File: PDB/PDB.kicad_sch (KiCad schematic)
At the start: 74 parts, among them J11 swd, J12 ESC - xt90, J13 ESC - xt90, J14 ESC - xt90, J15 ESC - xt90, J3 FC - XT30x1, J4 Sensors - XT30x1, J5 Jetson - XT60x1, J6 UART OUT, J7 Micro_SD_Card, J8 BATT_A - xt90, J9 BATT_B - xt90, Q5 IPT012N08N5, Q6 BSC093N15NS5, Q7 IPT012N08N5, Q8 BSC093N15NS5, U10 LTC4359-DCB, U11 LTC4359-DCB, U13 MCP9804_DFN, U14 MCP9804_DFN, U15 MCP9804_DFN, U2 STM32H742VGTx, U20 TMCS1108A4UQDRQ1

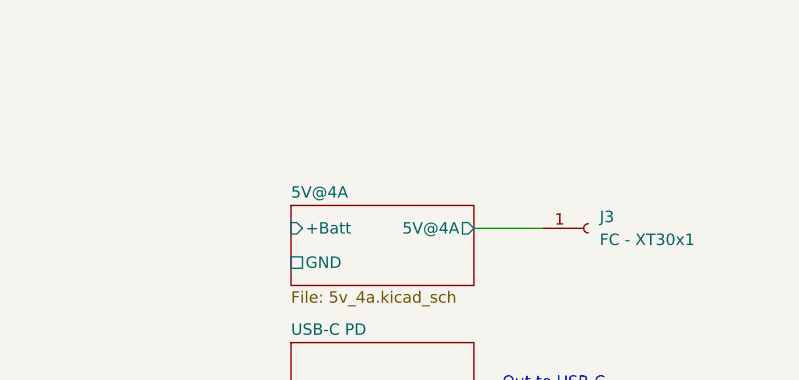
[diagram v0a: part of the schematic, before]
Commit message: finished the 12V@5A
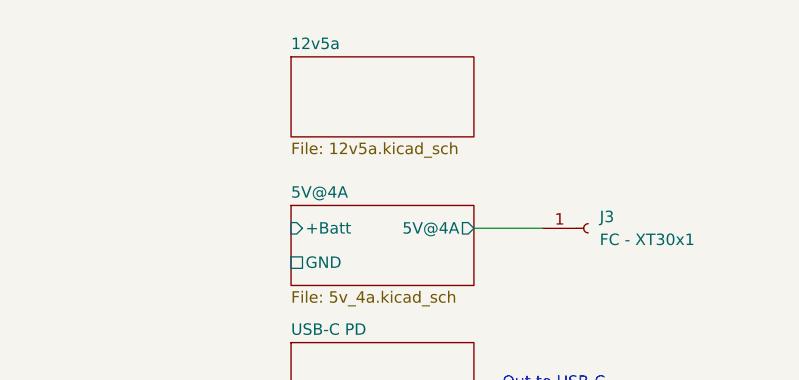
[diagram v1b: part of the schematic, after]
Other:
- added sheet 12v5a (12v5a.kicad_sch)
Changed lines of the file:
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@@
+	)
+	(sheet
+		(at 466.09 20.32)
+		(size 20.32 8.89)
+		(exclude_from_sim no)
+		(in_bom yes)
+		(on_board yes)
+		(dnp no)
+		(fields_autoplaced yes)
+		(stroke
+			(width 0.1524)
+			(type solid)
+		)
+		(fill
+			(color 0 0 0 0)
+		)
+		(property "Sheetname" "12v5a"
+			(at 466.09 19.6084 0)
+			(show_name no)
+			(do_not_autoplace no)
+			(effects
+				(font
+					(size 1.27 1.27)
+				)
+				(justify left bottom)
+			)
+		)
+		(property "Sheetfile" "12v5a.kicad_sch"
+			(at 466.09 29.7946 0)
+			(show_name no)
+			(do_not_autoplace no)
+			(effects
+				(font
+					(size 1.27 1.27)
+				)
+				(justify left top)
+			)
+		)
+		(instances
+			(project "PDB"
+				(path "/a9cf05c4-aac5-4cf1-b700-1d3045f8dfbd"
+					(page "7")
+				)
+			)
+		)
 	)
 	(sheet

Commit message: updated footprints
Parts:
- C10, C11, C13, C17, C19, C20, C21, C29, C30, C31, C37, C39, C8, C9: footprint Capacitor_SMD:C_1206_3216Metric -> Capacitor_SMD:C_0603_1608Metric
- J7: footprint (none) -> Connector_Card:microSD_HC_Hirose_DM3AT-SF-PEJM5
- R16, R27, R6, R8, R9: footprint Resistor_SMD:R_1206_3216Metric_Pad1.30x1.75mm_HandSolder -> Resistor_SMD:R_0603_1608Metric
- R19, R20, R21, R22, R23: footprint Resistor_SMD:R_0603_1608Metric_Pad0.98x0.95mm_HandSolder -> Resistor_SMD:R_0603_1608Metric
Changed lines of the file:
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@@
 			)
 		)
-		(property "Footprint" "Resistor_SMD:R_1206_3216Metric_Pad1.30x1.75mm_HandSolder"
+		(property "Footprint" "Resistor_SMD:R_0603_1608Metric"
 			(at 154.94 36.068 90)
 			(hide yes)
@@
 			)
 		)
-		(property "Footprint" "Capacitor_SMD:C_1206_3216Metric"
+		(property "Footprint" "Capacitor_SMD:C_0603_1608Metric"
 			(at 294.3352 110.49 0)
 			(hide yes)
@@
 			)
 		)
-		(property "Footprint" "Capacitor_SMD:C_1206_3216Metric"
+		(property "Footprint" "Capacitor_SMD:C_0603_1608Metric"
 			(at 167.9448 106.68 0)
 			(hide yes)
@@
 			)
 		)
-		(property "Footprint" "Resistor_SMD:R_0603_1608Metric_Pad0.98x0.95mm_HandSolder"
+		(property "Footprint" "Resistor_SMD:R_0603_1608Metric"
 			(at 87.63 210.312 90)
 			(hide yes)
@@
 			)
 		)
-		(property "Footprint" "Resistor_SMD:R_1206_3216Metric_Pad1.30x1.75mm_HandSolder"
+		(property "Footprint" "Resistor_SMD:R_0603_1608Metric"
 			(at 118.872 119.38 90)
 			(hide yes)
@@
 			)
 		)
-		(property "Footprint" "Capacitor_SMD:C_1206_3216Metric"
+		(property "Footprint" "Capacitor_SMD:C_0603_1608Metric"
 			(at 31.75 152.0952 0)
 			(hide yes)
@@
 			)
 		)
-		(property "Footprint" "Resistor_SMD:R_1206_3216Metric_Pad1.30x1.75mm_HandSolder"
+		(property "Footprint" "Resistor_SMD:R_0603_1608Metric"
 			(at 154.94 25.908 90)
 			(hide yes)
@@
 			)
 		)
-		(property "Footprint" "Capacitor_SMD:C_1206_3216Metric"
+		(property "Footprint" "Capacitor_SMD:C_0603_1608Metric"
 			(at 39.37 104.4448 0)
 			(hide yes)
@@
 			)
 		)
-		(property "Footprint" "Capacitor_SMD:C_1206_3216Metric"
+		(property "Footprint" "Capacitor_SMD:C_0603_1608Metric"
 			(at 295.6052 185.42 0)
 			(hide yes)
@@
 			)
 		)
-		(property "Footprint" "Capacitor_SMD:C_1206_3216Metric"
+		(property "Footprint" "Capacitor_SMD:C_0603_1608Metric"
 			(at 327.3552 64.77 0)
 			(hide yes)
@@
 			)
 		)
-		(property "Footprint" "Capacitor_SMD:C_1206_3216Metric"
+		(property "Footprint" "Capacitor_SMD:C_0603_1608Metric"
 			(at 327.3552 142.24 0)
 			(hide yes)
@@
 			)
 		)
-		(property "Footprint" "Capacitor_SMD:C_1206_3216Metric"
+		(property "Footprint" "Capacitor_SMD:C_0603_1608Metric"
 			(at 31.75 117.8052 0)
 			(hide yes)
@@
 			)
 		)
-		(property "Footprint" "Resistor_SMD:R_1206_3216Metric_Pad1.30x1.75mm_HandSolder"
+		(property "Footprint" "Resistor_SMD:R_0603_1608Metric"
 			(at 116.332 133.35 90)
 			(hide yes)
@@
 			)
 		)
-		(property "Footprint" ""
+		(property "Footprint" "Connector_Card:microSD_HC_Hirose_DM3AT-SF-PEJM5"
 			(at 151.13 218.44 0)
 			(hide yes)
@@
 			)
 		)
-		(property "Footprint" "Capacitor_SMD:C_1206_3216Metric"
+		(property "Footprint" "Capacitor_SMD:C_0603_1608Metric"
 			(at 31.75 82.2452 0)
 			(hide yes)
@@
 			)
 		)
-		(property "Footprint" "Resistor_SMD:R_0603_1608Metric_Pad0.98x0.95mm_HandSolder"
+		(property "Footprint" "Resistor_SMD:R_0603_1608Metric"
 			(at 87.63 201.422 90)
 			(hide yes)
@@
 			)
 		)
-		(property "Footprint" "Resistor_SMD:R_0603_1608Metric_Pad0.98x0.95mm_HandSolder"
+		(property "Footprint" "Resistor_SMD:R_0603_1608Metric"
 			(at 87.63 192.532 90)
 			(hide yes)
@@
 			)
 		)
-		(property "Footprint" "Capacitor_SMD:C_1206_3216Metric"
+		(property "Footprint" "Capacitor_SMD:C_0603_1608Metric"
 			(at 388.62 51.1048 0)
 			(hide yes)
@@
 			)
 		)
-		(property "Footprint" "Resistor_SMD:R_1206_3216Metric_Pad1.30x1.75mm_HandSolder"
+		(property "Footprint" "Resistor_SMD:R_0603_1608Metric"
 			(at 113.792 109.22 90)
 			(hide yes)
@@
 			)
 		)
-		(property "Footprint" "Capacitor_SMD:C_1206_3216Metric"
+		(property "Footprint" "Capacitor_SMD:C_0603_1608Metric"
 			(at 31.75 94.9452 0)
 			(hide yes)
@@
 			)
 		)
-		(property "Footprint" "Capacitor_SMD:C_1206_3216Metric"
+		(property "Footprint" "Capacitor_SMD:C_0603_1608Metric"
 			(at 31.75 140.6652 0)
 			(hide yes)
@@
 			)
 		)
-		(property "Footprint" "Resistor_SMD:R_0603_1608Metric_Pad0.98x0.95mm_HandSolder"
+		(property "Footprint" "Resistor_SMD:R_0603_1608Metric"
 			(at 87.63 183.642 90)
 			(hide yes)
@@
 			)
 		)
-		(property "Footprint" "Capacitor_SMD:C_1206_3216Metric"
+		(property "Footprint" "Capacitor_SMD:C_0603_1608Metric"
 			(at 170.4848 99.06 0)
 			(hide yes)
@@
 			)
 		)
-		(property "Footprint" "Capacitor_SMD:C_1206_3216Metric"
+		(property "Footprint" "Capacitor_SMD:C_0603_1608Metric"
 			(at 31.75 129.2352 0)
 			(hide yes)
@@
 			)
 		)
-		(property "Footprint" "Resistor_SMD:R_0603_1608Metric_Pad0.98x0.95mm_HandSolder"
+		(property "Footprint" "Resistor_SMD:R_0603_1608Metric"
 			(at 87.63 173.482 90)
 			(hide yes)

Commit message: Finished all the footprints. doing poe myself now
finally.
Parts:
- removed J12, J13, J14, J15: ESC - xt90, symbol Connector:Conn_01x01_Socket
- removed J3: FC - XT30x1, symbol Connector:Conn_01x01_Socket
- removed J4: Sensors - XT30x1, symbol Connector:Conn_01x01_Socket
- removed J5: Jetson - XT60x1, symbol Connector:Conn_01x01_Socket
- removed J8: BATT_A - xt90, symbol Connector:Conn_01x01_Socket
- removed J9: BATT_B - xt90, symbol Connector:Conn_01x01_Socket
- added J15, J16, J17, J18, J19, J20: XT90PW-M, Connector_AMASS:AMASS_XT90PW-M_1x02_P10.90mm_Horizontal, symbol sym&foot:XT90PW-M
- added J2, J3: XT30PW-M, Connector_AMASS:AMASS_XT30U-F_1x02_P5.0mm_Vertical, symbol sym&foot:XT90PW-M
- added J4: XT60PW-M, Connector_AMASS:AMASS_XT60-F_1x02_P7.20mm_Vertical, symbol sym&foot:XT90PW-M
- D10: renamed from D11; footprint (none) -> Diode_SMD:D_SOD-523
- D11: renamed from D14; footprint (none) -> Diode_SMD:D_SOD-523
- J6: footprint (none) -> Connector_PinHeader_2.54mm:PinHeader_1x04_P2.54mm_Vertical
- J9: renamed from J11; footprint (none) -> Connector_PinHeader_2.54mm:PinHeader_1x02_P2.54mm_Vertical
- S1: footprint EG1218:SW_EG1218 -> Dependencies:SW_EG1218
- renumbered C8 to C1, C39 to C10, C31 to C11, C29 to C12, C30 to C13, C37 to C14, C9 to C2, C11 to C3, C17 to C4, C19 to C5, C20 to C6, C21 to C7, C13 to C8, C10 to C9, D3 to D1, D5 to D2, D4 to D3, D6 to D4, D7 to D5, D9 to D6, D10 to D7, D12 to D8, D13 to D9, J7 to J1, Q5 to Q1, Q7 to Q2, Q6 to Q3, Q8 to Q4, R23 to R1, R27 to R10, R32 to R11, R33 to R12, R35 to R13, R31 to R14, R34 to R15, R36 to R16, R26 to R17, R29 to R18, R25 to R19, R22 to R2, R30 to R20, R21 to R3, R20 to R4, R19 to R5, R9 to R7, R16 to R9, TP5 to TP1, TP6 to TP2, TP1 to TP3, TP2 to TP4, TP3 to TP5, U2 to U1, U13 to U2, U14 to U3, U15 to U4, U10 to U5, U11 to U6, U20 to U7
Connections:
- net +BATT: now also J15.P (POS), J16.P (POS), J17.P (POS), J18.P (POS)
- net 3V3@1A/+3.3V@1A: now also J3.P (POS)
- net 5V@12A/5V@12A: now also J4.P (POS)
- net 5V@4A/5V@4A: now also J2.P (POS)
- net GND: now also J15.N (NEG), J16.N (NEG), J17.N (NEG), J18.N (NEG), J19.N (NEG), J2.N (NEG), J20.N (NEG), J3.N (NEG), J4.N (NEG)
- net batt_inA: now also J19.P (POS)
- net batt_inB: now also J20.P (POS)

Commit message: more footprint
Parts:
- U7: footprint TMCS1108A4UQDRQ1:SOIC127P599X175-8N -> Dependencies:SOIC127P599X175-8N
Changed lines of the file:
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@@
 			)
 		)
-		(property "Footprint" "TMCS1108A4UQDRQ1:SOIC127P599X175-8N"
+		(property "Footprint" "Dependencies:SOIC127P599X175-8N"
 			(at 365.76 64.77 0)
 			(hide yes)

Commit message: fixed component footprints
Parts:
- renumbered J18 to J10, J19 to J11, J20 to J12, J6 to J2, J9 to J3, J2 to J4, J3 to J5, J4 to J6, J15 to J7, J16 to J8, J17 to J9

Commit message: PoE+
Swap 24V for 48V and most of PoE+ controller is added with footprints for ic added
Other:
- sheet 24V@30W renamed 48V@.8A
- added sheet PoE+ (PoE+.kicad_sch)
- sheet 48V@.8A ports: added 48V@.8A; removed 24V@1.5A
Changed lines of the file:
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@@
 	(text "Out to RJ45\n"
 		(exclude_from_sim no)
-		(at 495.554 89.408 0)
+		(at 541.02 88.138 0)
 		(effects
 			(font
@@
 	)
 	(sheet
+		(at 498.475 85.09)
+		(size 25.4 11.43)
+		(exclude_from_sim no)
+		(in_bom yes)
+		(on_board yes)
+		(dnp no)
+		(fields_autoplaced yes)
+		(stroke
+			(width 0.1524)
+			(type solid)
+		)
+		(fill
+			(color 0 0 0 0)
+		)
+		(property "Sheetname" "PoE+"
+			(at 498.475 84.3784 0)
+			(show_name no)
+			(do_not_autoplace no)
+			(effects
+				(font
+					(size 1.27 1.27)
+				)
+				(justify left bottom)
+			)
+		)
+		(property "Sheetfile" "PoE+.kicad_sch"
+			(at 498.475 97.1046 0)
+			(show_name no)
+			(do_not_autoplace no)
+			(effects
+				(font
+					(size 1.27 1.27)
+				)
+				(justify left top)
+			)
+		)
+		(instances
+			(project "PDB"
+				(path "/a9cf05c4-aac5-4cf1-b700-1d3045f8dfbd"
+					(page "8")
+				)
+			)
+		)
+	)
+	(sheet
 		(at 466.09 85.09)
 		(size 20.32 8.89)
@@
 			(color 0 0 0 0)
 		)
-		(property "Sheetname" "24V@30W"
+		(property "Sheetname" "48V@.8A"
 			(at 466.09 84.3784 0)
 			(show_name no)
@@
 			)
 		)
-		(pin "24V@1.5A" output
+		(pin "48V@.8A" output
 			(at 486.41 87.63 0)
 			(effects

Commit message: worked on more layout
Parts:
- removed R12, R13, R15, R16: 10k, Resistor_SMD:R_0603_1608Metric_Pad0.98x0.95mm_HandSolder, symbol Device:R

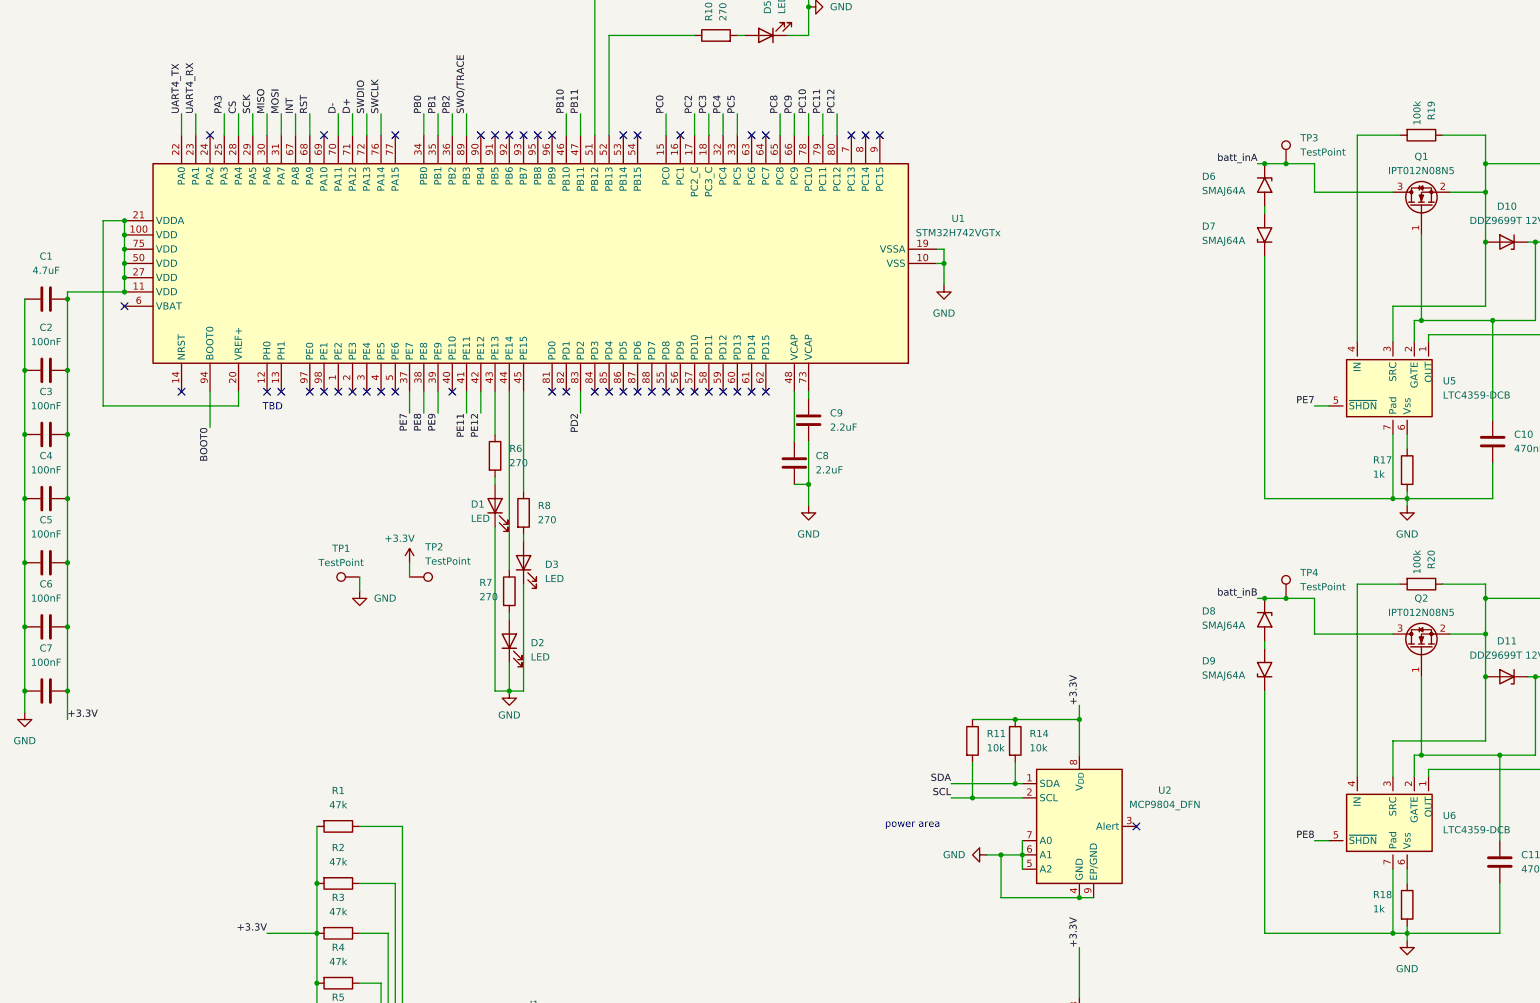
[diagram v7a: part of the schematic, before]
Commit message: coordinated labels in schem
Labeled all components to be Rxx, Cxx, ext forms through all sheets so labels for BOM and layout are work together as one long list.
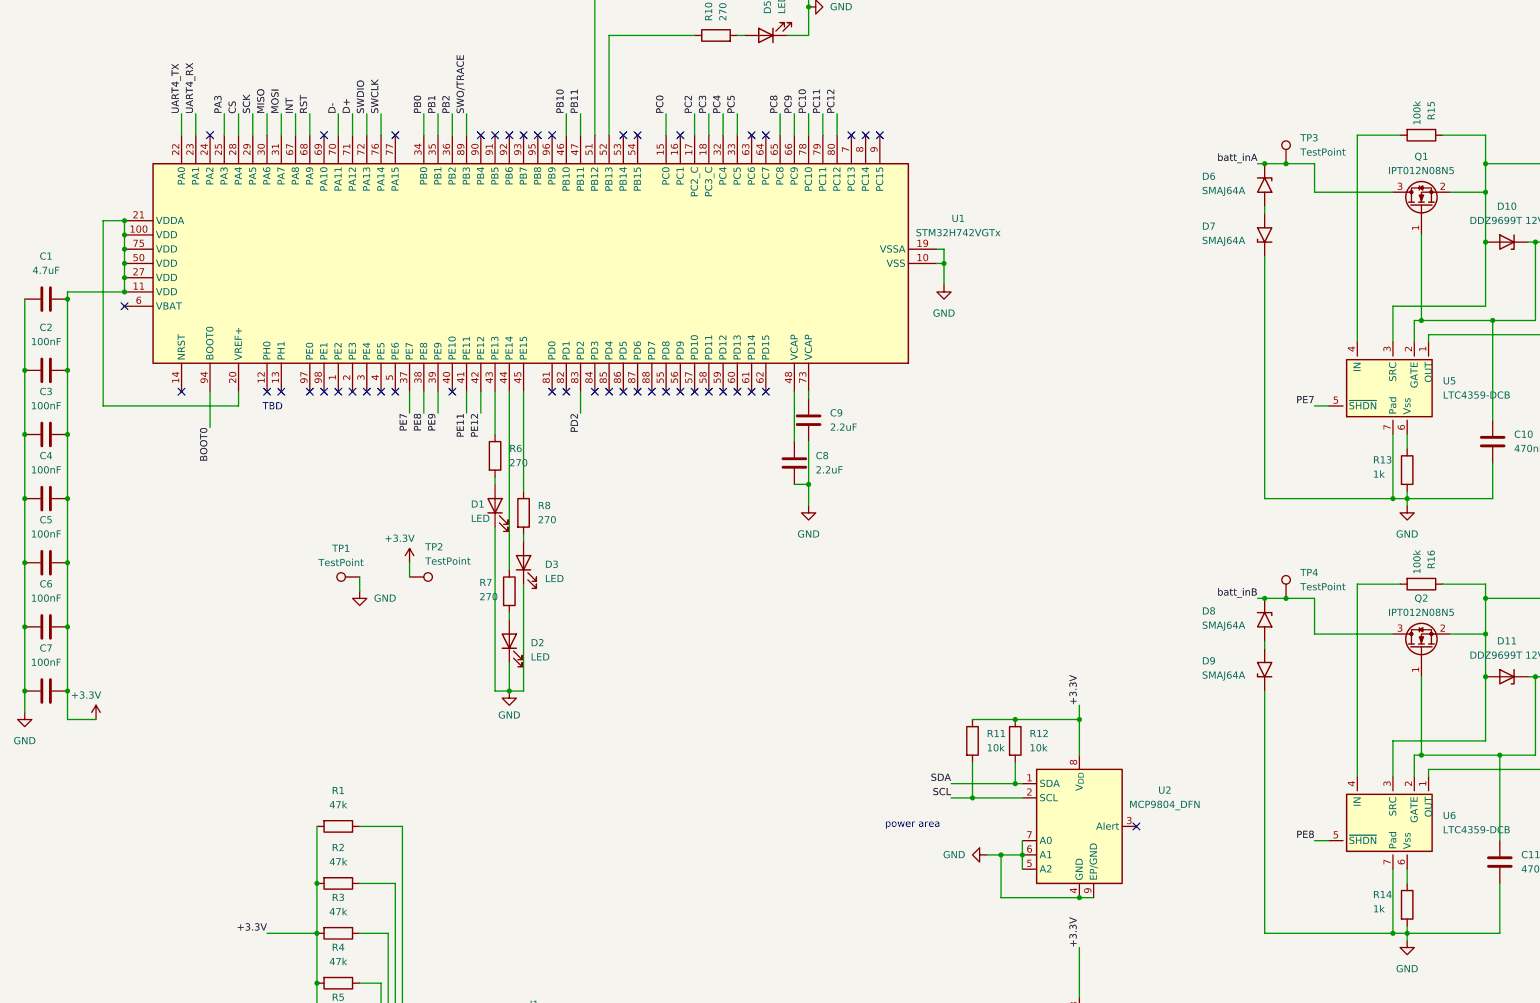
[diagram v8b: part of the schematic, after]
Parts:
- renumbered R14 to R12, R17 to R13, R18 to R14, R19 to R15, R20 to R16
